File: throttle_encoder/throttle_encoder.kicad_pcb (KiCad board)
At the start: 4 copper layers, 40 x 40 mm, 31 parts, among them J1 DSUB-9, P1 USB_C_Receptacle, P2 TC2030-CTX, SW1 INTERLOCK, SW2 SW_SPST, U2 TCAN1044VDDFR, U3 STM32G0B1KBUx, U4 AP2112K-3.3, Y2 ABS07-32.768kHz

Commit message: Finishing touches
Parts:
- removed the SW1 at (123.9, 134.6)
- added J2: 2601-1102, railspeeder:CONN2_2601-1102_WAG, F.Cu at (120.2, 132.2)
- FL1: footprint Inductor_SMD:L_CommonModeChoke_Coilcraft_0603USB -> railspeeder:DLW32PH_MUR
- moved R2 6.29 mm to (129.2, 117.2), turned to 0 degrees
- moved C7 3.55 mm to (126.5, 112.2), turned to 0 degrees
- moved C13 2.55 mm to (128.8, 112.2), turned to 180 degrees
- moved U3 2.26 mm to (128.8, 114.7)
- moved FL1 0.86 mm to (123.8, 114.8), turned to 180 degrees
- moved D1 0.82 mm to (116.6, 114.8)
- moved C10 0.82 mm to (118.7, 116.2)
- moved C12 0.82 mm to (118.7, 114.8)
- moved C4 0.82 mm to (118.7, 113.2)
- moved R1 0.82 mm to (120.2, 113.8)
- moved R6 0.82 mm to (120.2, 115.8)
- renumbered C5 to C1, C17 to C11, C1 to C12, C2 to C13, C4 to C2, C14 to C3, C9 to C4, C13 to C5, C3 to C7, C7 to C9, P2 to P1, P1 to P2, R3 to R2, R6 to R3, R7 to R4, R8 to R5, R2 to R6, SW2 to SW1, U4 to U1, U3 to U2, U2 to U3, Y2 to Y1
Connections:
- FL1 pad 1: Net-(U2-CANL) -> Net-(U3-CANH)
- FL1 pad 2: /CANL -> /CANH
- FL1 pad 3: /CANH -> /CANL
- FL1 pad 4: Net-(U2-CANH) -> Net-(U3-CANL)
- U3 pad 6: Net-(U2-CANL) -> Net-(U3-CANL)
- U3 pad 7: Net-(U2-CANH) -> Net-(U3-CANH)
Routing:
- net +5V: track 75.8 -> 71.0 mm, vias 0 -> 4
- net /INTERLOCK: track 33.2 -> 36.1 mm
- net +3V3: track 13.9 -> 11.0 mm, vias 5 -> 6
- net Net-(U3-CANH): track 0.00 -> 1.97 mm
- net Net-(U3-CANL): track 0.00 -> 1.94 mm
- net Net-(U2-CANH): track 1.47 -> 0.00 mm
- net /CANTX: track 17.3 -> 18.6 mm
- net Net-(U2-CANL): track 1.27 -> 0.00 mm
- net GND: track 29.2 -> 28.0 mm
- net /CAN_STB: track 1.46 -> 2.18 mm

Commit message: Finishing touches
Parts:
- renumbered C9 to C10, C10 to C11, C11 to C12, C12 to C13, C13 to C9
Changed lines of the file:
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@@
 		(tags "resistor")
 		(property "Reference" "R2"
-			(at 0.5 1.5 360)
+			(at 0.5 1.5 0)
 			(layer "F.SilkS")
 			(effects
@@
 		)
 		(property "Value" "5.1k"
-			(at 0 1.17 360)
+			(at 0 1.17 0)
 			(layer "F.Fab")
 			(effects
@@
 		)
 		(fp_text user "${REFERENCE}"
-			(at 0 0 360)
+			(at 0 0 0)
 			(layer "F.Fab")
 			(effects
@@
 		(descr "Capacitor SMD 0402 (1005 Metric), square (rectangular) end terminal, IPC_7351 nominal, (Body size source: IPC-SM-782 page 76, https://www.pcb-3d.com/wordpress/wp-content/uploads/ipc-sm-782a_amendment_1_and_2.pdf), generated with kicad-footprint-generator")
 		(tags "capacitor")
-		(property "Reference" "C10"
+		(property "Reference" "C11"
 			(at 2.55 -0.325 0)
 			(layer "F.SilkS")
@@
 		(descr "Capacitor SMD 0402 (1005 Metric), square (rectangular) end terminal, IPC_7351 nominal, (Body size source: IPC-SM-782 page 76, https://www.pcb-3d.com/wordpress/wp-content/uploads/ipc-sm-782a_amendment_1_and_2.pdf), generated with kicad-footprint-generator")
 		(tags "capacitor")
-		(property "Reference" "C11"
+		(property "Reference" "C12"
 			(at 2.6 -0.1 0)
 			(layer "F.SilkS")
@@
 		(descr "Capacitor SMD 0402 (1005 Metric), square (rectangular) end terminal, IPC_7351 nominal, (Body size source: IPC-SM-782 page 76, https://www.pcb-3d.com/wordpress/wp-content/uploads/ipc-sm-782a_amendment_1_and_2.pdf), generated with kicad-footprint-generator")
 		(tags "capacitor")
-		(property "Reference" "C12"
+		(property "Reference" "C13"
 			(at 0.55 2.675 0)
 			(layer "F.SilkS")
@@
 		(tags "capacitor")
 		(property "Reference" "C7"
-			(at -0.48 -1.25 360)
+			(at -0.48 -1.25 0)
 			(layer "F.SilkS")
 			(effects
@@
 		)
 		(property "Value" "0.1uF"
-			(at 0 1.16 360)
+			(at 0 1.16 0)
 			(layer "F.Fab")
 			(effects
@@
 		)
 		(fp_text user "${REFERENCE}"
-			(at 0 0 360)
+			(at 0 0 0)
 			(layer "F.Fab")
 			(effects
@@
 		)
 		(property "Footprint" "railspeeder:DLW32PH_MUR"
-			(at 0 0 360)
+			(at 0 0 0)
 			(layer "F.Fab")
 			(hide yes)
@@
 		)
 		(property "Datasheet" "DLW32SH510XF2L"
-			(at 0 0 360)
+			(at 0 0 0)
 			(layer "F.Fab")
 			(hide yes)
@@
 		)
 		(property "Description" "Common mode choke, 500mA, 250VAC, 98nH, 174mohm, 1.9Ghz,"
-			(at 0 0 360)
+			(at 0 0 0)
 			(layer "F.Fab")
 			(hide yes)
@@
 		(descr "Capacitor SMD 0402 (1005 Metric), square (rectangular) end terminal, IPC_7351 nominal, (Body size source: IPC-SM-782 page 76, https://www.pcb-3d.com/wordpress/wp-content/uploads/ipc-sm-782a_amendment_1_and_2.pdf), generated with kicad-footprint-generator")
 		(tags "capacitor")
-		(property "Reference" "C13"
+		(property "Reference" "C9"
 			(at 0 1.25 180)
 			(layer "F.SilkS")
@@
 		)
 		(property "Value" "0.1uF"
-			(at 0 1.16 360)
+			(at 0 1.16 0)
 			(layer "F.Fab")
 			(effects
@@
 		)
 		(fp_text user "${REFERENCE}"
-			(at 0 0 360)
+			(at 0 0 0)
 			(layer "F.Fab")
 			(effects
@@
 		(descr "Capacitor SMD 0402 (1005 Metric), square (rectangular) end terminal, IPC_7351 nominal, (Body size source: IPC-SM-782 page 76, https://www.pcb-3d.com/wordpress/wp-content/uploads/ipc-sm-782a_amendment_1_and_2.pdf), generated with kicad-footprint-generator")
 		(tags "capacitor")
-		(property "Reference" "C9"
+		(property "Reference" "C10"
 			(at 1.88 1.0625 180)
 			(layer "F.SilkS")

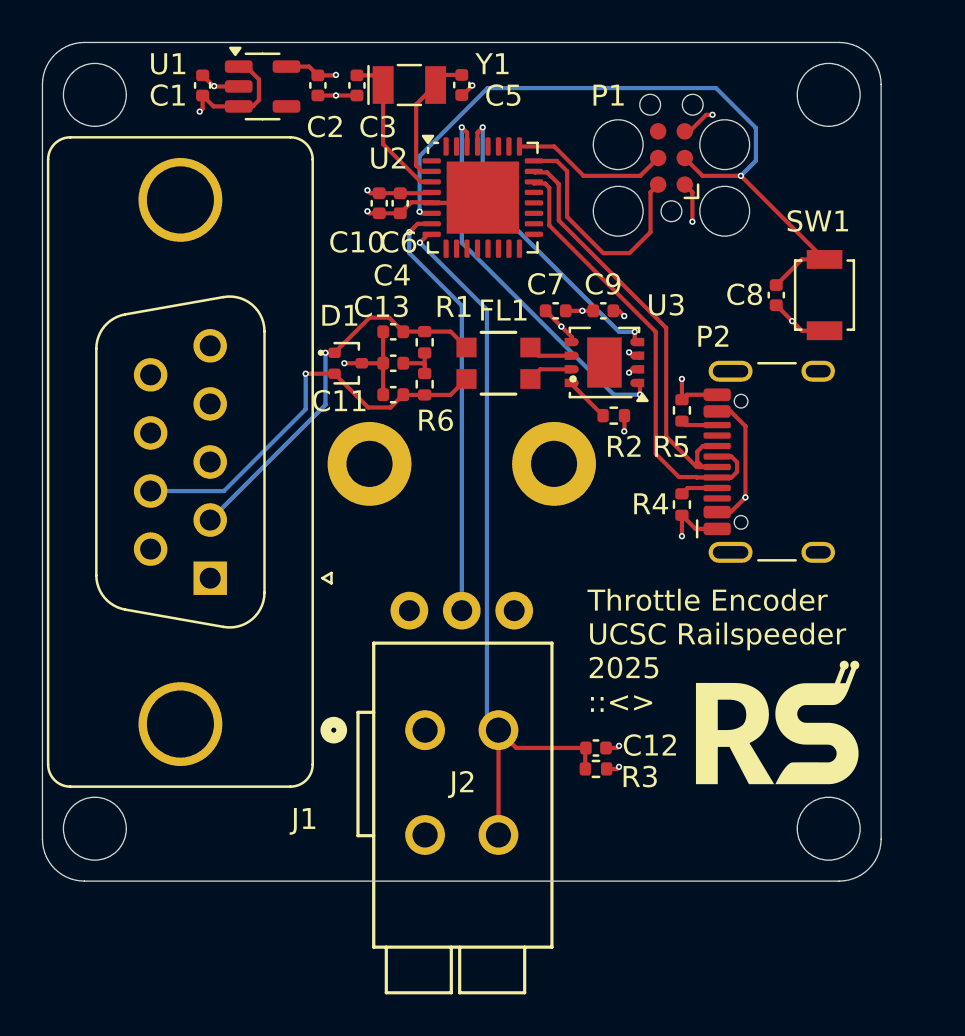
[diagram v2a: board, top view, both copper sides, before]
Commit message: Sweeping via resizing
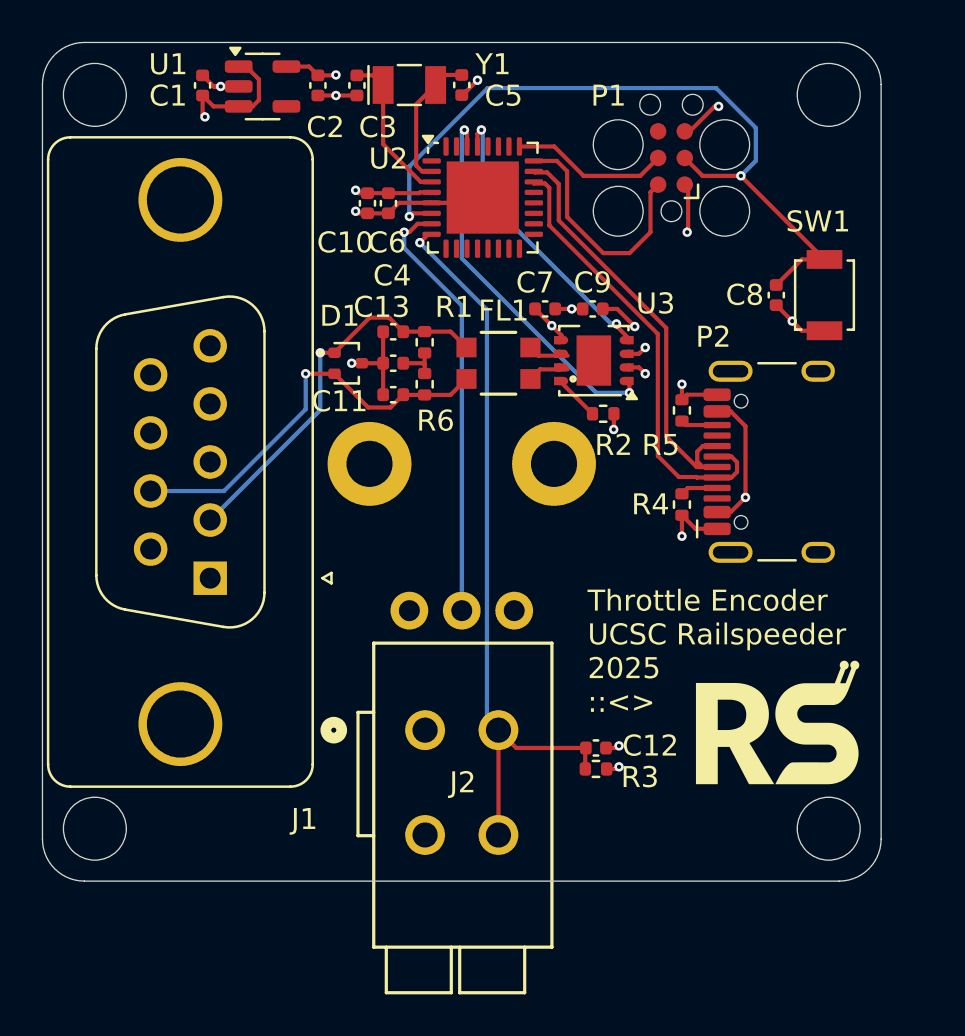
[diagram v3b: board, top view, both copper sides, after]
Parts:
- moved C10 0.56 mm to (117.5, 107.1)
- moved C6 0.56 mm to (118.5, 107.1)
- moved C7 0.51 mm to (126.0, 112.2)
- moved C9 0.51 mm to (128.2, 112.2)
- moved R2 0.51 mm to (128.7, 117.2)
- moved U3 0.51 mm to (128.3, 114.6)
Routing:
- net +5V: track 71.0 -> 65.8 mm
- net GND: track 28.0 -> 29.3 mm
- net +3V3: track 11.0 -> 12.1 mm
- net /NRST: track 35.5 -> 36.4 mm
- net /CANRX: track 14.7 -> 14.0 mm
